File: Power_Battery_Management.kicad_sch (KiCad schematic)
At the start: 32 parts, among them J501 Solder Wire Pad 1,5x3mm, J502 S2B-PH-SM4-TB, J503 Solder Wire Pad 1,5x3mm, Q501 NMOS IRLML6344TRPBF SOT-23, Q502 CSD85302L, U501 BQ29737DSER, U502 MCP73831T-2ACI/MC

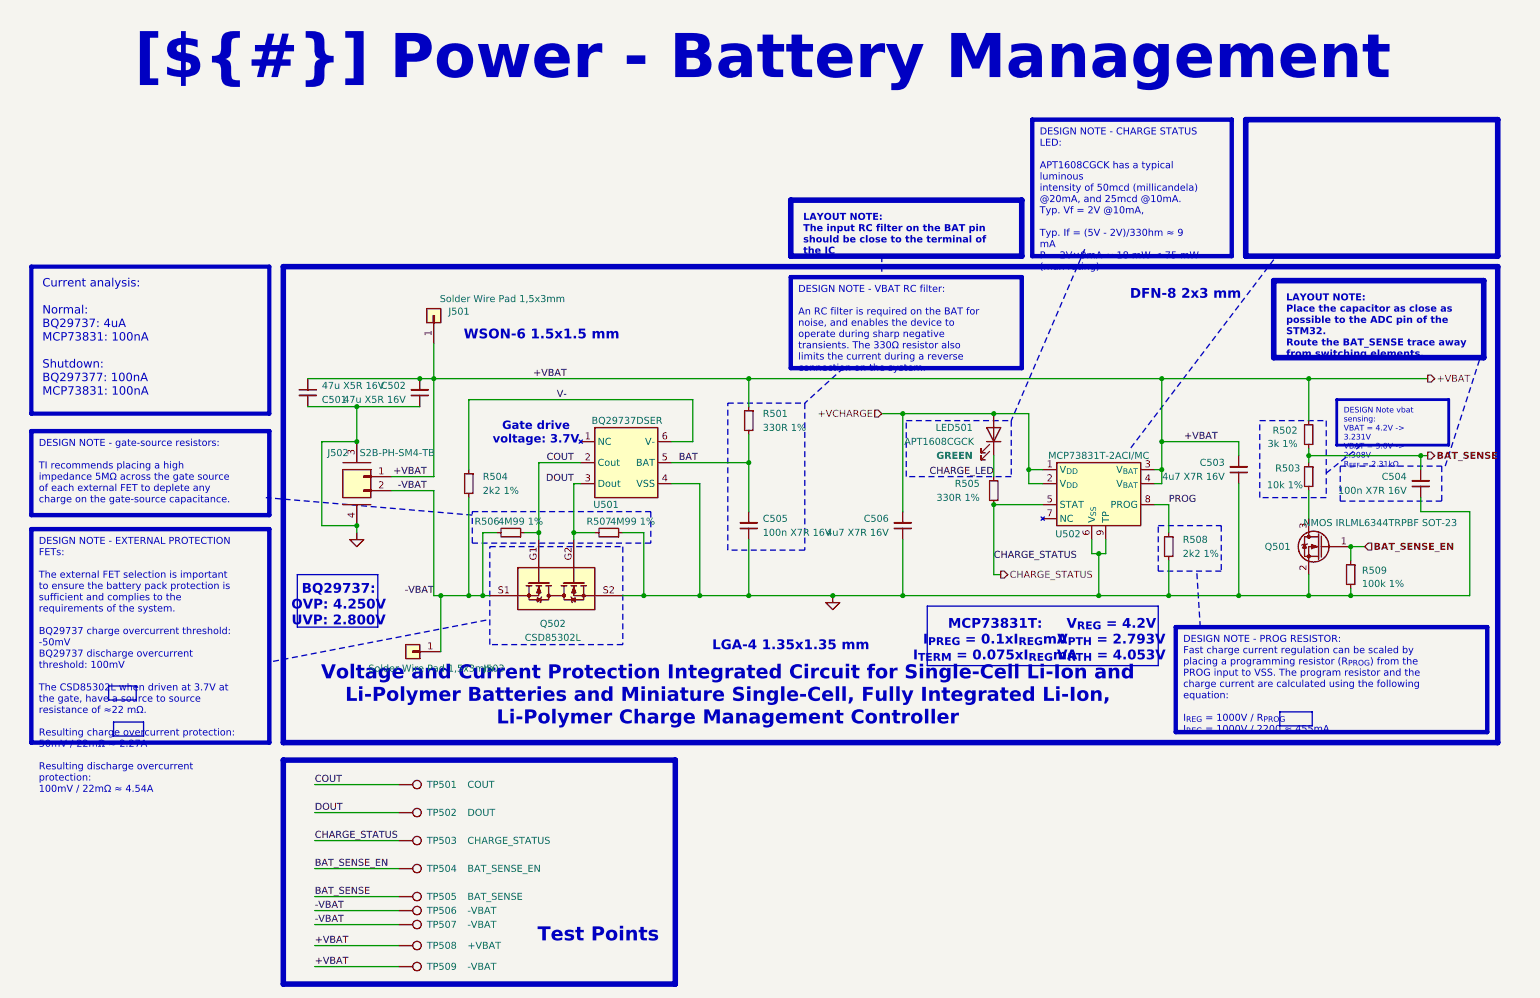
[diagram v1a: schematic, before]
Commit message: Added PCB frame for assembly, almost finished auto-review, only MCU and motors left
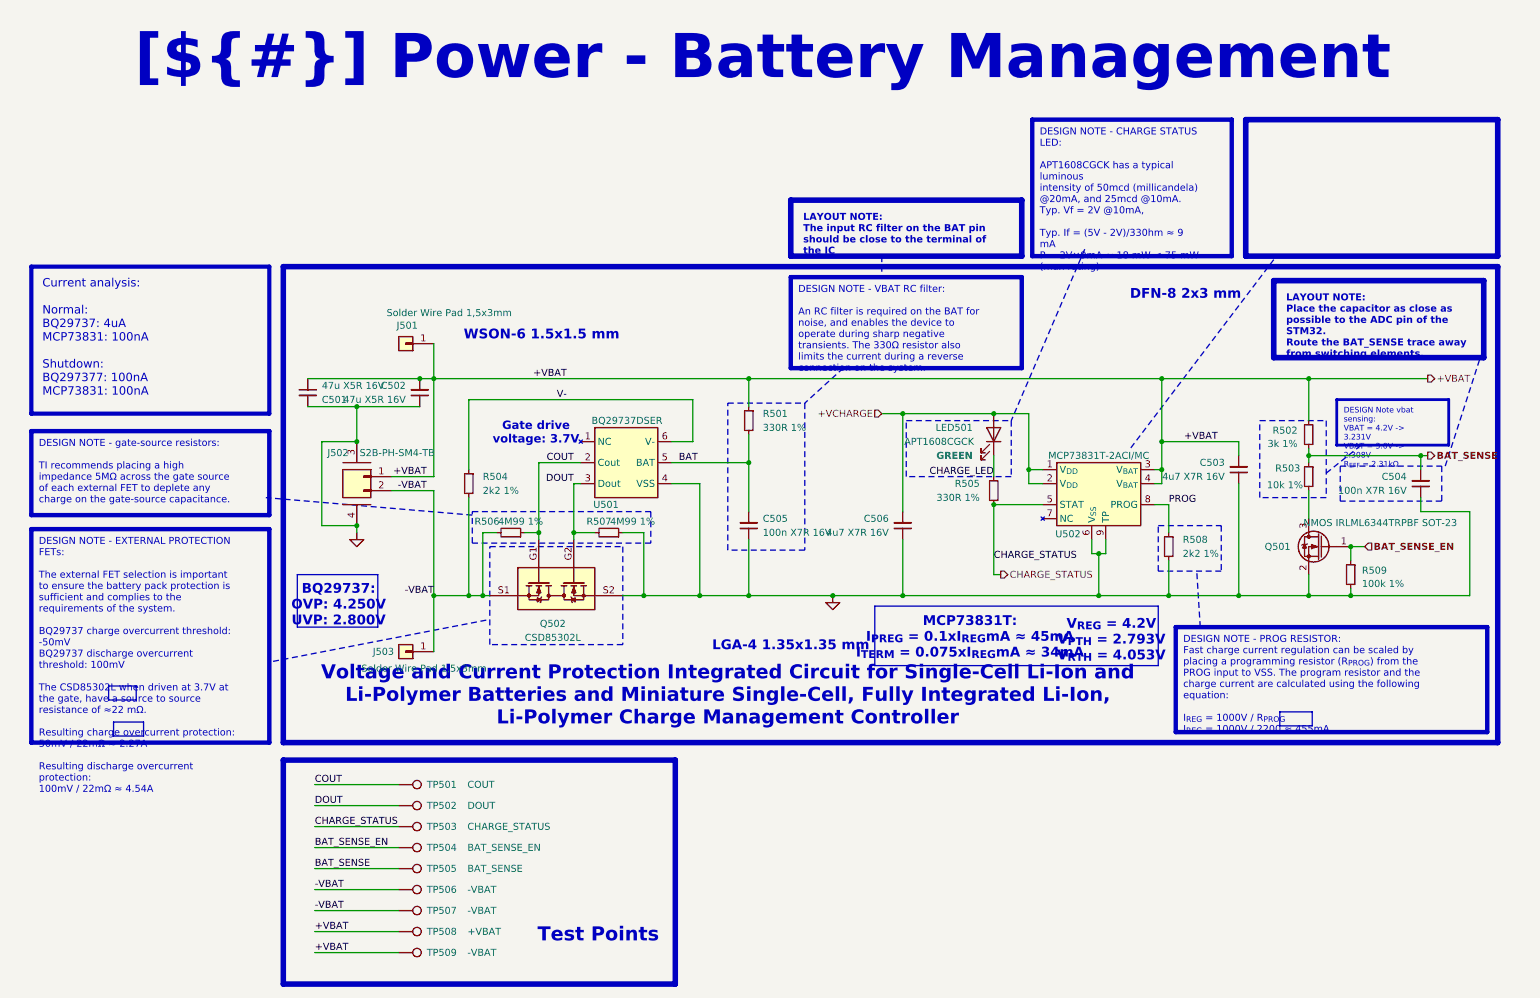
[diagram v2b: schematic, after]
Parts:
- TP501, TP502, TP503, TP504, TP505: footprint 0_Plume:TestPoint_Pad_D0.5mm_Back -> 0_Plume:TestPoint_Pad_D0.5mm_Front
- TP506, TP508: footprint 0_Plume:TestPoint_Pad_D0.5mm_Back -> 0_Plume:TestPoint_Pad_D0.75mm_Front
- U501: footprint Package_SON:WSON-6_1.5x1.5mm_P0.5mm -> 0_Plume:WSON-6_1.5x1.5mm_P0.5mm
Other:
- note added: "MCP73831T: I_{PREG} = 0.1xI_{REG}mA ≈ 45mA I_{TERM} = 0.075xI_{REG}mA ≈ 34mA"
- note removed: "MCP73831T: I_{PREG} = 0.1xI_{REG}mA I_{TERM} = 0.075xI_{REG}mA"
- moved on the sheet: J501, J503, TP502, TP503, TP504, TP505, TP506, TP507, TP508, TP509

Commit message: Final version, cleaned and ordered as is
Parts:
- J502: Manufacturer JST Sales America Inc. -> JST Commercial; Manufacturer Part Number S2B-PH-SM4-TB -> S2B-PH-SM4-TB(LF)(SN); Supplier Digikey -> Mouser Electronics; Supplier Part Number 455-S2B-PH-SM4-TBCT-ND -> 306-S2BPHSM4TBLFSN
